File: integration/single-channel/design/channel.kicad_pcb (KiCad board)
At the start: 4 copper layers, 164 x 90 mm, 52 parts, among them J1 MCX edge jack 50R, J2 MCX edge jack 50R, J3 MCX edge jack 50R, J4 MCX edge jack 50R, J5 Screw terminal 3-pos 5.08mm, U1 CR-112, U2 CR-200-1us, U3 CR-210, U4 THS3491

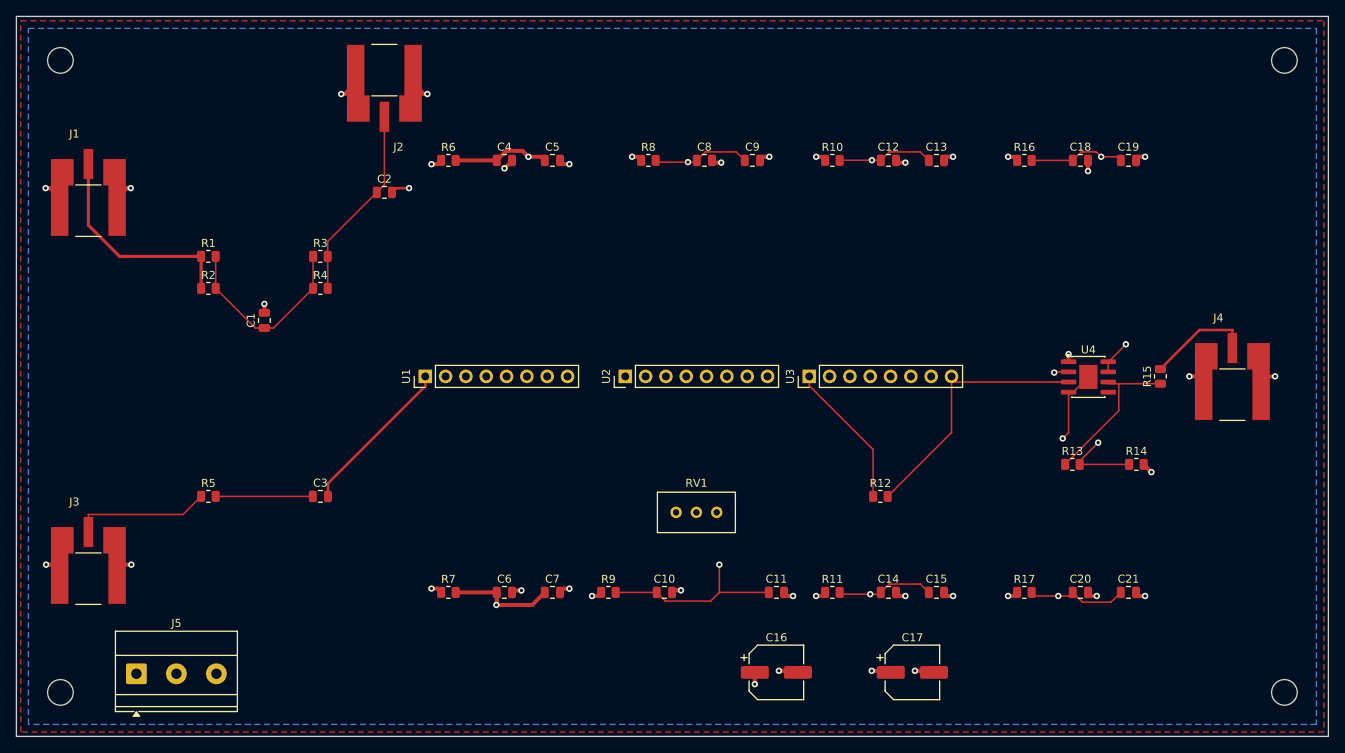
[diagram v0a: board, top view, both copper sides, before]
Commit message: Single-channel PCB: rebuild as a thin, tile-able channel-row cell (DRC 0/0/0)
Lay out channel.kicad_pcb per the requested floorplan: each channel is a horizontal ROW
(signal left->right: front-end -> CR-112 -> CR-200 -> CR-210 -> THS3491), the four MCX
edge-mount female jacks at the two SHORT ends (left = SIPM(IN)+TEST_IN, right = OUT_50+BIAS_IN),
and a shared COM row across the top (screw terminal + F1/F2 PTC + D1/D2 Schottky + C10/C11 bulk,
power in at the rear). Channels stack below the COM row for the multi-channel board. Thin:
138 x 52 mm (the stacked MCX-pair height sets the ~24 mm channel row).

- gen_pcb.py: new PLACE / W,H / DNP_BY_REF for the floorplan + the 2026-07 refs (F1/F2/D1/D2,
  R18=JP_BUF, buffer-block DNP set); net-class patterns for *VDC_IN*/*VDC_F*; 2 M3 holes in the
  COM row; hide J1-J4/R2/R4/R13 silk refs for a clean F.Silkscreen.
- Fully autorouted (FreeRouting 2.2.4, needs Java 25; score 996.4), 171 tracks / 41 vias,
  4-layer (F.Cu / In1=GND / In2=-VDC / B.Cu=+VDC pour). DRC 0 errors / 0 warnings / 0 unconnected.
- Docs (INTERFACE.md, SESSION_REPORT.md, SESSION_LOG.md) updated: PCB no longer stale; mechanical
  section now describes the thin channel-row cell + tiling.

GUI finishing left: restore the 4 MCX Edge.Cuts cutouts at the true board edges (parked on
Dwgs.User); optional per-connector silk function labels.

Co-Authored-By: Claude Opus 4.8 <noreply@anthropic.com>
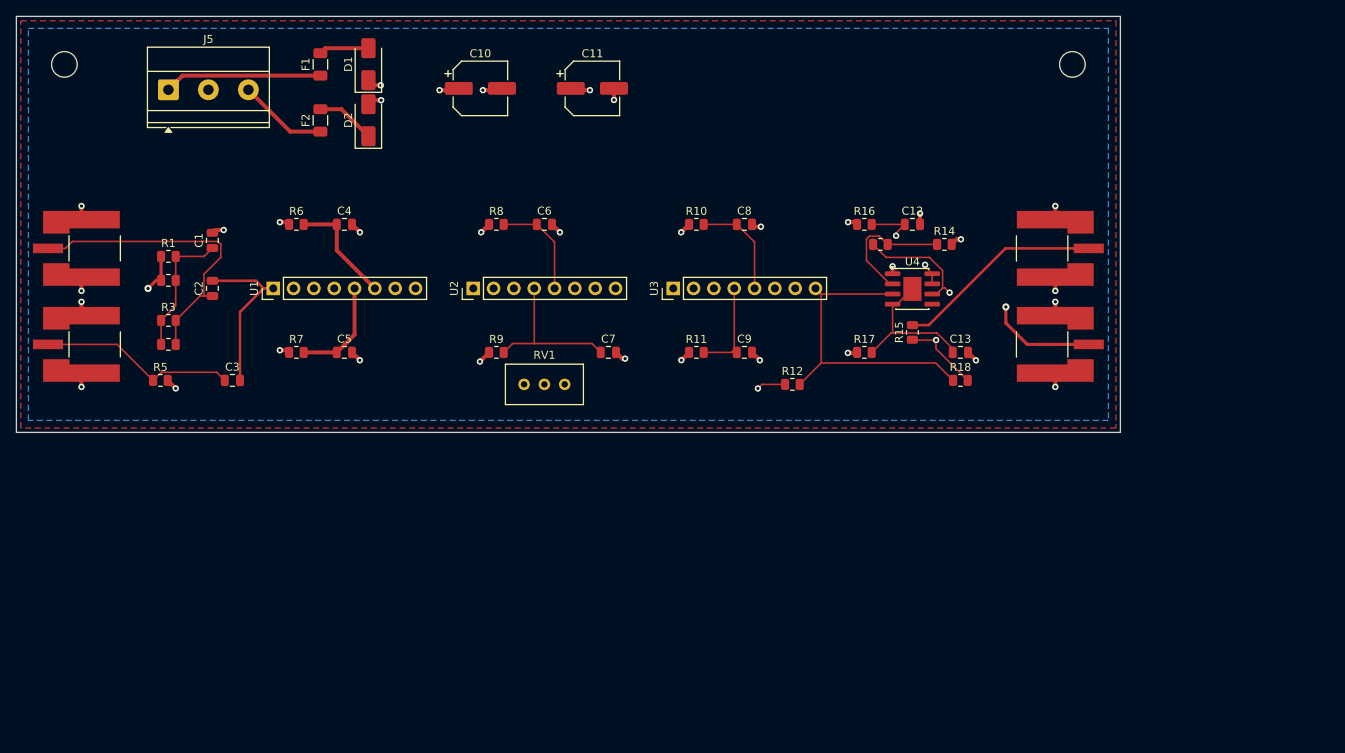
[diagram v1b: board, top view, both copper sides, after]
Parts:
- removed C14, C18, C20: 10uF 25V X5R, C_0805_2012Metric
- removed C15, C19, C21: 0.1uF 50V X7R, C_0805_2012Metric
- removed C16, C17: 100uF 35V, CP_Elec_6.3x7.7
- removed H3, H4: MountingHole_3.2mm_M3, MountingHole_3.2mm_M3
- added D1: SS14, D_SMA, F.Cu at (44.0, 5.98)
- added D2: SS14, D_SMA, F.Cu at (44.0, 13.0)
- added F1: PTC 0.1A, Fuse_1206_3216Metric, F.Cu at (38.0, 6.00)
- added F2: PTC 0.1A, Fuse_1206_3216Metric, F.Cu at (38.0, 13.0)
- added R18: 0R, R_0805_2012Metric, F.Cu at (118.0, 45.5)
- C10: value 10uF 25V X5R -> 100uF 35V; footprint C_0805_2012Metric -> CP_Elec_6.3x7.7
- C11: value 0.1uF 50V X7R -> 100uF 35V; footprint C_0805_2012Metric -> CP_Elec_6.3x7.7
- C13, C5, C7, C9: value 0.1uF 50V X7R -> 10uF 25V X5R
- moved J1 124.0 mm to (131.4, 41.0), turned to -90 degrees
- moved J5 73.1 mm to (19.0, 9.17)
- moved C10 67.1 mm to (58.0, 9.00)
- moved C11 67.1 mm to (72.0, 9.00)
- moved C6 46.3 mm to (66.0, 26.0)
- moved J2 43.8 mm to (6.63, 29.0), turned to 90 degrees
- moved R13 36.5 mm to (108.0, 28.5)
- moved R14 36.5 mm to (116.0, 28.5)
- moved R17 36.1 mm to (106.0, 42.0)
- moved R7 35.5 mm to (35.0, 42.0)
- moved C5 35.4 mm to (41.0, 42.0)
- moved R11 34.5 mm to (85.0, 42.0)
- moved R9 33.1 mm to (60.0, 42.0)
- moved R15 31.5 mm to (112.0, 39.5)
- moved C7 30.8 mm to (74.0, 42.0)
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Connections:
- C10 pad 1: /SHVN -> +VDC
- C11 pad 1: /SHVN -> GND
- C11 pad 2: GND -> -VDC
- C12 pad 1: /BLVP -> /BVP
- C13 pad 1: /BLVP -> /BVN
- C3 pad 1: /TEST_N -> /TEST_IN
- C5 pad 1: /+VS_F -> /-VS_F
- C6 pad 1: /-VS_F -> /SHVP
- C7 pad 1: /-VS_F -> /SHVN
- C8 pad 1: /SHVP -> /BLVP
- C9 pad 1: /SHVP -> /BLVN
- J5 pad 1: +VDC -> /+VDC_IN
- J5 pad 3: -VDC -> /-VDC_IN
- R5 pad 2: /TEST_N -> GND
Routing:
- net /BIAS_IN: track 27.4 -> 126.7 mm, vias 0 -> 2
- net /-VS_F: track 42.5 -> 13.1 mm, vias 1 -> 0
- net /SHVN: track 49.4 -> 19.9 mm, vias 1 -> 0
- net /BLVN: track 39.4 -> 12.1 mm, vias 1 -> 0
- net /BVP: track 41.1 -> 13.9 mm
- net /BLVP: track 40.0 -> 13.1 mm, vias 1 -> 0
- net /SHVP: track 39.9 -> 13.1 mm, vias 1 -> 0
- net /CSP_IN: track 46.8 -> 20.7 mm, vias 1 -> 0
- net /+VS_F: track 39.7 -> 14.1 mm, vias 1 -> 0
- net /BVN: track 41.8 -> 19.3 mm, vias 2 -> 0
- net /+VDC_IN: track 0.00 -> 19.7 mm
- net /FE: track 24.4 -> 38.3 mm
- net /OUT_50: track 13.3 -> 26.0 mm
- net /TEST_N: track 12.1 -> 0.00 mm
- net /BUF_OUT: track 19.5 -> 31.2 mm, vias 0 -> 2
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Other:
- board size 164 x 90 mm -> 138 x 52 mm
